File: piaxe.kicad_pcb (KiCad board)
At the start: 4 copper layers, 85 x 56 mm, 94 parts, among them J1 Barrel_Jack_Switch, J2 Conn_02x20_Odd_Even, J3 Conn_01x05, J5 temp, M1 Fan_4pin, Q1 CSD16321Q5, Q2 CSD16321Q5, Q3 BSS138, Q4 BSS138, Q5 BSS138, Q9 BSS138, U1 TPS40304DRC, U14 BM1366_mode1, U5 MCP1824T-1802E, U6 MCP1824T-0802E, U7 25MHz

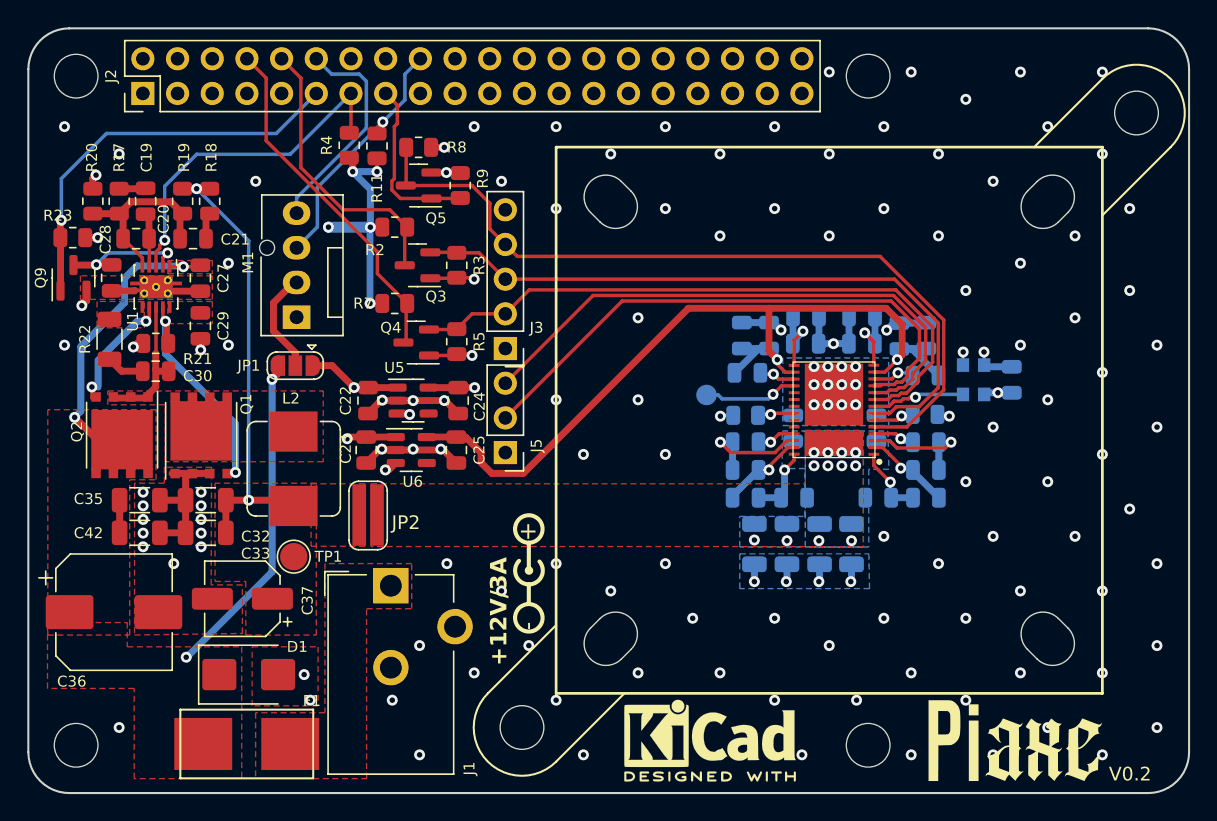
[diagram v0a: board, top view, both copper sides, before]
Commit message: fixed some order numbers, added initial python code for testing
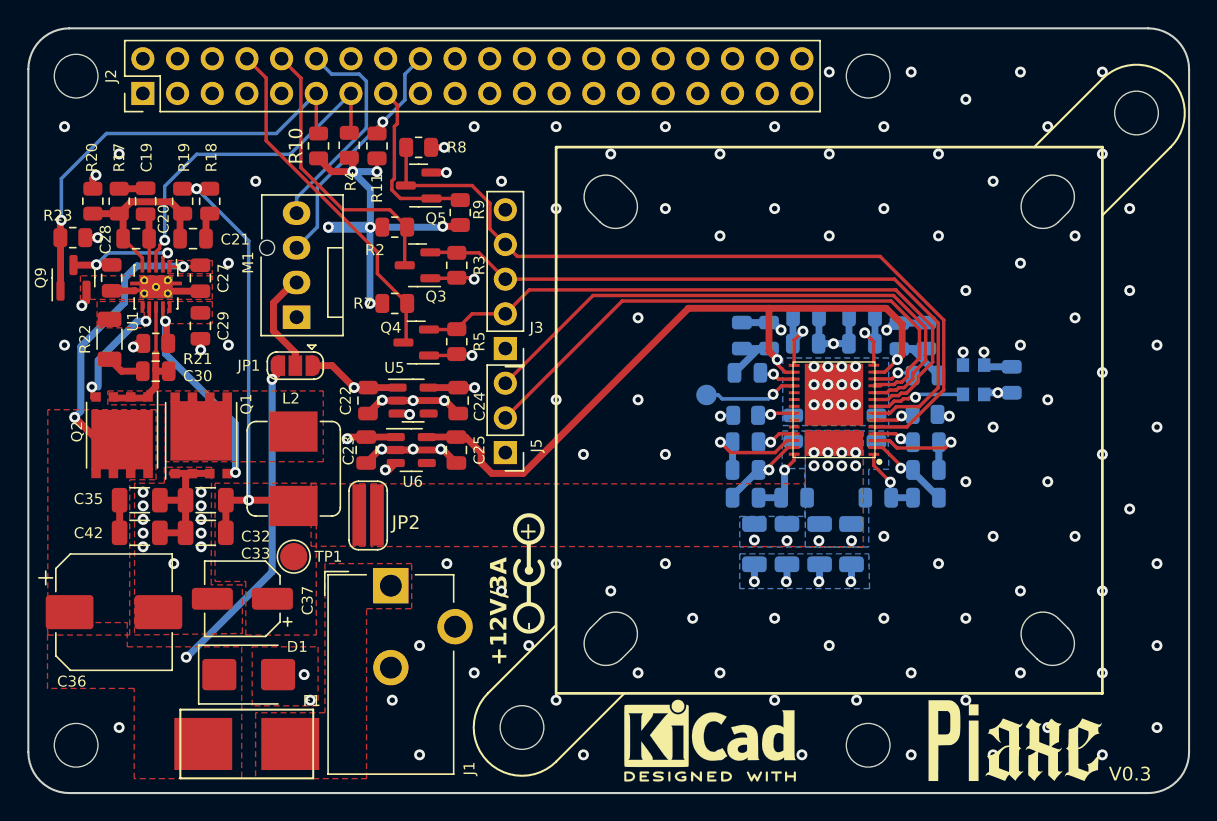
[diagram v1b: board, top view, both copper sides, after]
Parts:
- added R10: 100k, Resistor_SMD:R_0805_2012Metric, F.Cu at (194.6, 64.4)
- moved R9 1.98 mm to (205.0, 69.3)
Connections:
- R9 pad 1: GND -> /Pi/NRST
- R9 pad 2: /Pi/NRST -> +3V3
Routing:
- net +3V3: track 38.4 -> 47.9 mm, vias 5 -> 6
- net /Pi/SDN: track 29.5 -> 32.5 mm
- net GND: track 108.3 -> 107.3 mm
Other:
- board text added: "V0.3"
- board text removed: "V0.2"
